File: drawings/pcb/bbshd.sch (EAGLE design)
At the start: 53 parts, among them IC1 LM358D

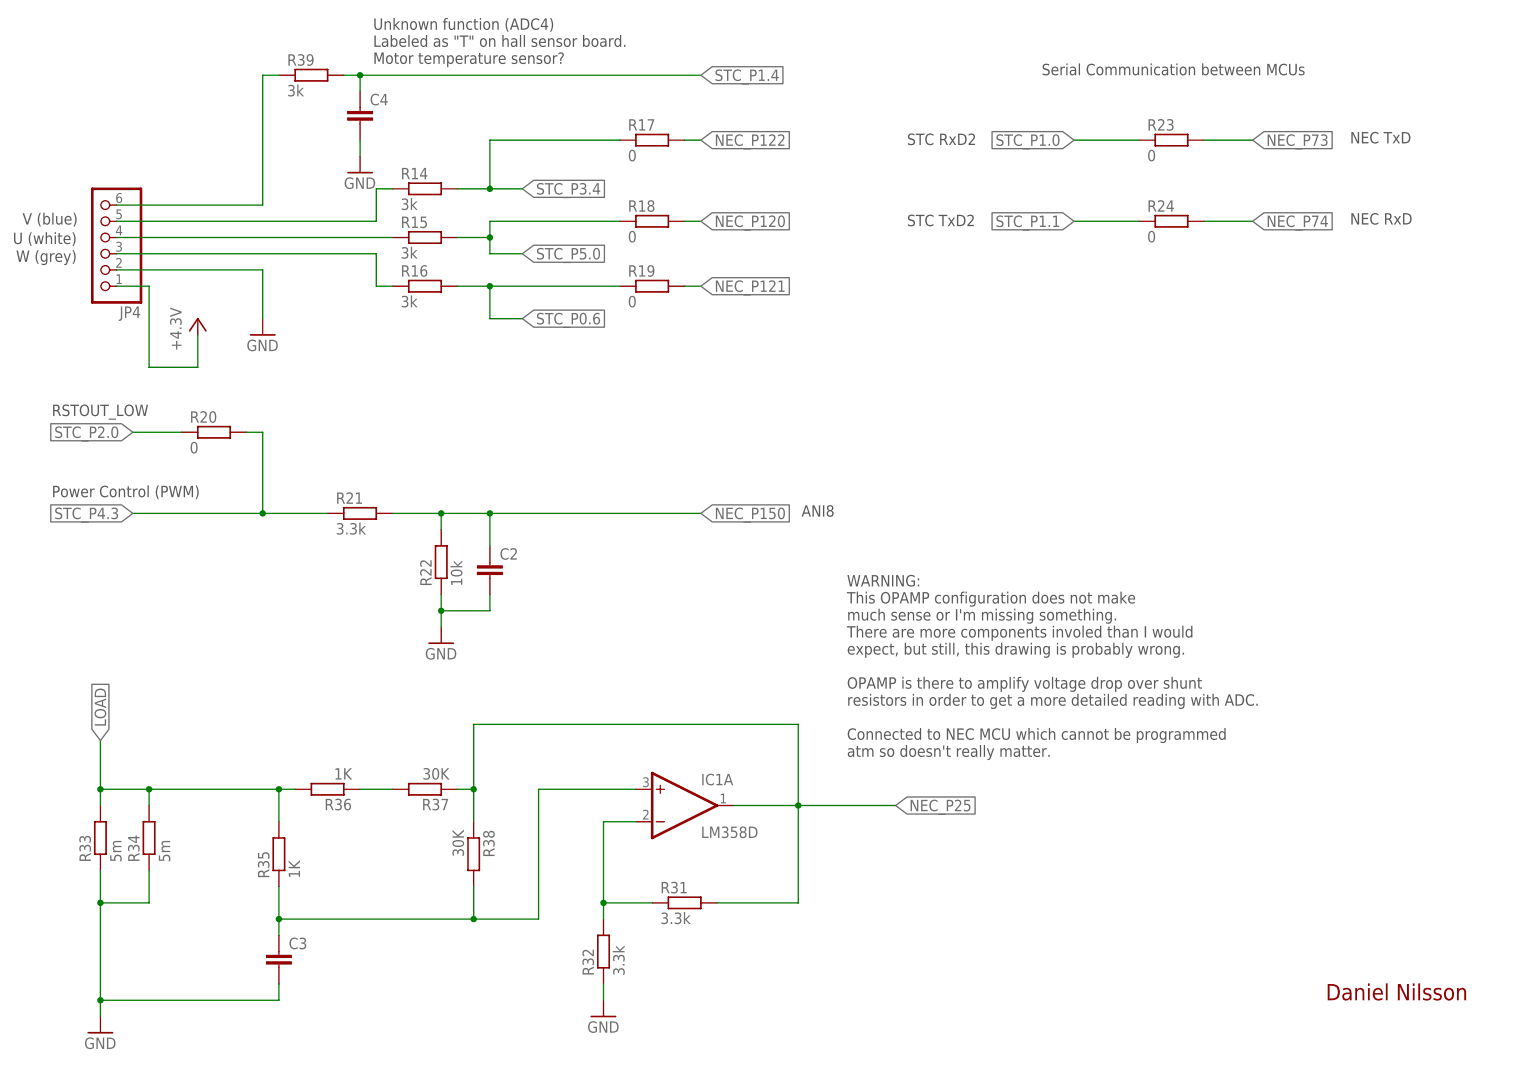
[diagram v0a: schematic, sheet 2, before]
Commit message: Updated shematic for opamp current senser circuit, should be more correct now. Added code dump of 79F9211 ebike controller found on chinese website
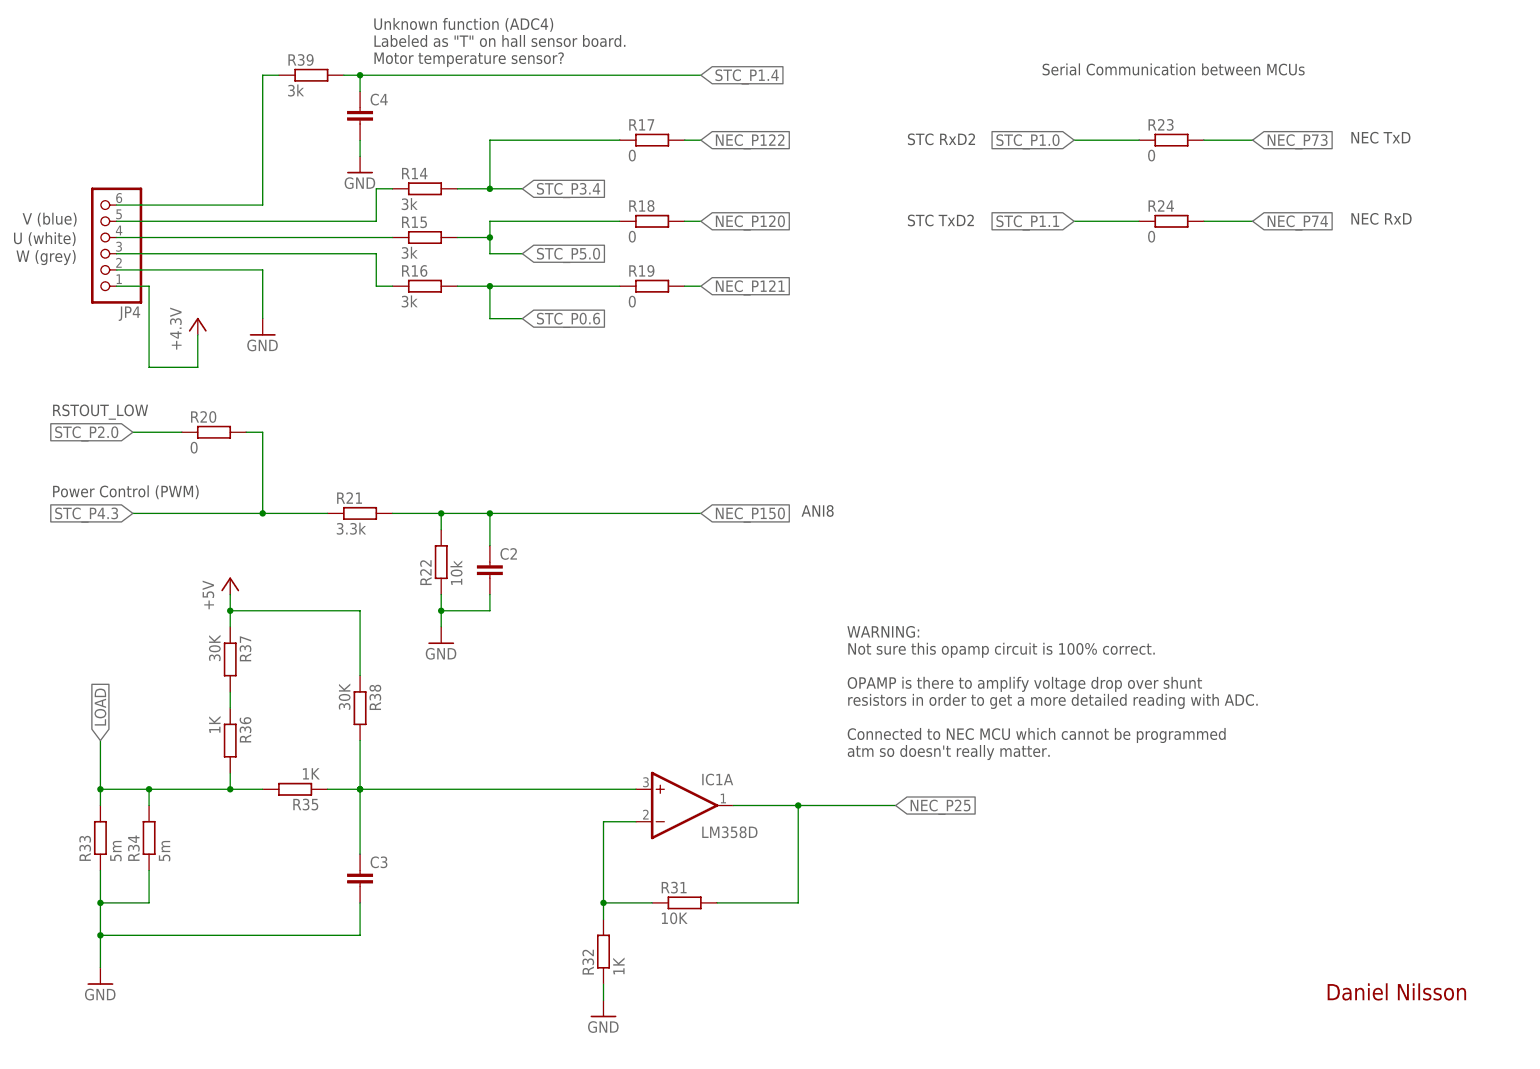
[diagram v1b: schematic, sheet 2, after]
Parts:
- R31: value 3.3k -> 10K
- R32: value 3.3k -> 1K
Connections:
- net +5V: now also R37.1, R38.1
- net NEC_P25: no longer R37.1, R38.1
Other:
- note added: "WARNING: Not sure this opamp circuit is 100% correct. OPAMP is there to amplify voltage drop over shunt resistors in order to get a more detailed reading with ADC. Connected to NEC MCU which cannot be programmed atm so doesn't really matter."
- note removed: "WARNING: This OPAMP configuration does not make much sense or I'm missing something. There are more components involed than I would expect, but still, this drawing is probably wrong. OPAMP is there to amplify voltage drop over shunt resistors in order to get a more detailed reading with ADC. Connected to NEC MCU which cannot be programmed atm so doesn't really matter."
- moved on the sheet: C3, R35, R36, R37, R38
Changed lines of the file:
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@@
 <part name="R30" library="rcl" deviceset="R-EU_" device="R0603" value="2.0K"/>
 <part name="IC1" library="linear" deviceset="LM358" device="D"/>
-<part name="R31" library="rcl" deviceset="R-EU_" device="R0603" value="3.3k"/>
-<part name="R32" library="rcl" deviceset="R-EU_" device="R0603" value="3.3k"/>
+<part name="R31" library="rcl" deviceset="R-EU_" device="R0603" value="10K"/>
+<part name="R32" library="rcl" deviceset="R-EU_" device="R0603" value="1K"/>
 <part name="GND9" library="supply1" deviceset="GND" device=""/>
 <part name="R33" library="rcl" deviceset="R-EU_" device="R0603" value="5m"/>
@@
 <part name="C4" library="rcl" deviceset="C-EU" device="C0603"/>
 <part name="GND11" library="supply1" deviceset="GND" device=""/>
+<part name="P+6" library="supply1" deviceset="+5V" device=""/>
 </parts>
 <sheets>
@@
 <text x="217.17" y="20.32" size="2.54" layer="94">Daniel Nilsson</text>
 <text x="142.24" y="58.42" size="1.778" layer="97">WARNING:
-This OPAMP configuration does not make
-much sense or I'm missing something.
-There are more components involed than I would
-expect, but still, this drawing is probably wrong.
+Not sure this opamp circuit is 100% correct.
 OPAMP is there to amplify voltage drop over shunt
 resistors in order to get a more detailed reading with ADC.
@@
 <instance part="R33" gate="G$1" x="25.4" y="45.72" rot="R90"/>
 <instance part="R34" gate="G$1" x="33.02" y="45.72" rot="R90"/>
-<instance part="GND10" gate="1" x="25.4" y="15.24"/>
-<instance part="C3" gate="G$1" x="53.34" y="27.94"/>
-<instance part="R35" gate="G$1" x="53.34" y="43.18" rot="R90"/>
-<instance part="R36" gate="G$1" x="60.96" y="53.34" rot="R180"/>
-<instance part="R37" gate="G$1" x="76.2" y="53.34" rot="R180"/>
-<instance part="R38" gate="G$1" x="83.82" y="43.18" rot="R270"/>
+<instance part="GND10" gate="1" x="25.4" y="22.86"/>
+<instance part="C3" gate="G$1" x="66.04" y="40.64"/>
+<instance part="R35" gate="G$1" x="55.88" y="53.34" rot="R180"/>
+<instance part="R36" gate="G$1" x="45.72" y="60.96" rot="R270"/>
+<instance part="R37" gate="G$1" x="45.72" y="73.66" rot="R270"/>
+<instance part="R38" gate="G$1" x="66.04" y="66.04" rot="R270"/>
 <instance part="R39" gate="G$1" x="58.42" y="165.1"/>
 <instance part="C4" gate="G$1" x="66.04" y="160.02"/>
 <instance part="GND11" gate="1" x="66.04" y="149.86"/>
+<instance part="P+6" gate="1" x="45.72" y="86.36"/>
 </instances>
 <busses>
@@
 <wire x1="25.4" y1="35.56" x2="25.4" y2="40.64" width="0.1524" layer="91"/>
 <pinref part="GND10" gate="1" pin="GND"/>
-<wire x1="25.4" y1="35.56" x2="25.4" y2="20.32" width="0.1524" layer="91"/>
+<wire x1="25.4" y1="35.56" x2="25.4" y2="30.48" width="0.1524" layer="91"/>
 <junction x="25.4" y="35.56"/>
+<wire x1="25.4" y1="30.48" x2="25.4" y2="25.4" width="0.1524" layer="91"/>
+<wire x1="66.04" y1="30.48" x2="25.4" y2="30.48" width="0.1524" layer="91"/>
+<junction x="25.4" y="30.48"/>
 <pinref part="C3" gate="G$1" pin="2"/>
-<wire x1="25.4" y1="20.32" x2="25.4" y2="17.78" width="0.1524" layer="91"/>
-<wire x1="53.34" y1="22.86" x2="53.34" y2="20.32" width="0.1524" layer="91"/>
-<wire x1="53.34" y1="20.32" x2="25.4" y2="20.32" width="0.1524" layer="91"/>
-<junction x="25.4" y="20.32"/>
+<wire x1="66.04" y1="35.56" x2="66.04" y2="30.48" width="0.1524" layer="91"/>
 </segment>
 <segment>
@@
 <wire x1="25.4" y1="50.8" x2="25.4" y2="53.34" width="0.1524" layer="91"/>
 <junction x="25.4" y="53.34"/>
+<junction x="33.02" y="53.34"/>
+<wire x1="45.72" y1="55.88" x2="45.72" y2="53.34" width="0.1524" layer="91"/>
 <pinref part="R36" gate="G$1" pin="2"/>
-<wire x1="55.88" y1="53.34" x2="53.34" y2="53.34" width="0.1524" layer="91"/>
-<junction x="33.02" y="53.34"/>
 <pinref part="R35" gate="G$1" pin="2"/>
-<wire x1="53.34" y1="53.34" x2="33.02" y2="53.34" width="0.1524" layer="91"/>
-<wire x1="53.34" y1="48.26" x2="53.34" y2="53.34" width="0.1524" layer="91"/>
-<junction x="53.34" y="53.34"/>
-</segment>
-</net>
-<net name="N$19" class="0">
-<segment>
-<pinref part="R36" gate="G$1" pin="1"/>
-<pinref part="R37" gate="G$1" pin="2"/>
-<wire x1="66.04" y1="53.34" x2="71.12" y2="53.34" width="0.1524" layer="91"/>
+<wire x1="45.72" y1="53.34" x2="33.02" y2="53.34" width="0.1524" layer="91"/>
+<wire x1="50.8" y1="53.34" x2="45.72" y2="53.34" width="0.1524" layer="91"/>
+<junction x="45.72" y="53.34"/>
 </segment>
 </net>
 <net name="NEC_P25" class="0">
 <segment>
-<pinref part="R37" gate="G$1" pin="1"/>
-<wire x1="81.28" y1="53.34" x2="83.82" y2="53.34" width="0.1524" layer="91"/>
-<pinref part="R38" gate="G$1" pin="1"/>
-<wire x1="83.82" y1="53.34" x2="83.82" y2="48.26" width="0.1524" layer="91"/>
-<wire x1="83.82" y1="53.34" x2="83.82" y2="63.5" width="0.1524" layer="91"/>
-<junction x="83.82" y="53.34"/>
 <pinref part="IC1" gate="A" pin="OUT"/>
 <wire x1="124.46" y1="50.8" x2="134.62" y2="50.8" width="0.1524" layer="91"/>
@@
 <pinref part="R31" gate="G$1" pin="2"/>
 <wire x1="134.62" y1="35.56" x2="121.92" y2="35.56" width="0.1524" layer="91"/>
-<wire x1="83.82" y1="63.5" x2="134.62" y2="63.5" width="0.1524" layer="91"/>
-<wire x1="134.62" y1="63.5" x2="134.62" y2="50.8" width="0.1524" layer="91"/>
 <junction x="134.62" y="50.8"/>
 <wire x1="134.62" y1="50.8" x2="149.86" y2="50.8" width="0.1524" layer="91"/>
 <label x="149.86" y="50.8" size="1.778" layer="95" xref="yes"/>
-</segment>
-</net>
-<net name="N$21" class="0">
-<segment>
-<pinref part="R38" gate="G$1" pin="2"/>
-<wire x1="83.82" y1="38.1" x2="83.82" y2="33.02" width="0.1524" layer="91"/>
-<wire x1="83.82" y1="33.02" x2="53.34" y2="33.02" width="0.1524" layer="91"/>
-<pinref part="R35" gate="G$1" pin="1"/>
-<pinref part="C3" gate="G$1" pin="1"/>
-<wire x1="53.34" y1="38.1" x2="53.34" y2="33.02" width="0.1524" layer="91"/>
-<wire x1="53.34" y1="33.02" x2="53.34" y2="30.48" width="0.1524" layer="91"/>
-<junction x="53.34" y="33.02"/>
-<pinref part="IC1" gate="A" pin="+IN"/>
-<wire x1="109.22" y1="53.34" x2="93.98" y2="53.34" width="0.1524" layer="91"/>
-<wire x1="93.98" y1="53.34" x2="93.98" y2="33.02" width="0.1524" layer="91"/>
-<wire x1="93.98" y1="33.02" x2="83.82" y2="33.02" width="0.1524" layer="91"/>
-<junction x="83.82" y="33.02"/>
 </segment>
 </net>
@@
 </segment>
 </net>
+<net name="N$18" class="0">
+<segment>
+<pinref part="R37" gate="G$1" pin="2"/>
+<pinref part="R36" gate="G$1" pin="1"/>
+<wire x1="45.72" y1="68.58" x2="45.72" y2="66.04" width="0.1524" layer="91"/>
+</segment>
+</net>
+<net name="+5V" class="0">
+<segment>
+<pinref part="P+6" gate="1" pin="+5V"/>
+<pinref part="R37" gate="G$1" pin="1"/>
+<wire x1="45.72" y1="83.82" x2="45.72" y2="81.28" width="0.1524" layer="91"/>
+<pinref part="R38" gate="G$1" pin="1"/>
+<wire x1="45.72" y1="81.28" x2="45.72" y2="78.74" width="0.1524" layer="91"/>
+<wire x1="66.04" y1="71.12" x2="66.04" y2="81.28" width="0.1524" layer="91"/>
+<wire x1="66.04" y1="81.28" x2="45.72" y2="81.28" width="0.1524" layer="91"/>
+<junction x="45.72" y="81.28"/>
+</segment>
+</net>
+<net name="N$19" class="0">
+<segment>
+<pinref part="C3" gate="G$1" pin="1"/>
+<pinref part="R35" gate="G$1" pin="1"/>
+<wire x1="60.96" y1="53.34" x2="66.04" y2="53.34" width="0.1524" layer="91"/>
+<pinref part="R38" gate="G$1" pin="2"/>
+<wire x1="66.04" y1="53.34" x2="66.04" y2="43.18" width="0.1524" layer="91"/>
+<wire x1="66.04" y1="60.96" x2="66.04" y2="53.34" width="0.1524" layer="91"/>
+<junction x="66.04" y="53.34"/>
+<wire x1="66.04" y1="53.34" x2="109.22" y2="53.34" width="0.1524" layer="91"/>
+<junction x="66.04" y="53.34"/>
+<pinref part="IC1" gate="A" pin="+IN"/>
+</segment>
+</net>

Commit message: Add more relevant documentation for 79F9211 controller. Updated schematic drawing with motor enable signal. Added some original bafang firmware dumps.
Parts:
- added LED1: (no value), led:LED
- added R40: 5.6K, rcl:R-EU_R0603
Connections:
- new net N$20: LED1.C, R40.1
- new net NEC_P70: R40.2
- net +5V: now also LED1.A
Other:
- note added: "Active High"
- note added: "Motor Enable"
- note added: "Some form of status LED. Seems to be blinking during normal operation."
- note removed: "ANI8"
- note removed: "Power Control (PWM)"
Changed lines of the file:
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@@
 <part name="GND11" library="supply1" deviceset="GND" device=""/>
 <part name="P+6" library="supply1" deviceset="+5V" device=""/>
+<part name="P+7" library="supply1" deviceset="+5V" device=""/>
+<part name="R40" library="rcl" deviceset="R-EU_" device="R0603" value="5.6K"/>
+<part name="LED1" library="led" deviceset="LED" device=""/>
 </parts>
 <sheets>
@@
 <text x="13.208" y="141.732" size="1.778" layer="97">V (blue)</text>
 <text x="12.192" y="135.89" size="1.778" layer="97">W (grey)</text>
-<text x="17.78" y="99.06" size="1.778" layer="97">Power Control (PWM)</text>
+<text x="17.78" y="99.06" size="1.778" layer="97">Motor Enable</text>
 <text x="17.78" y="111.76" size="1.778" layer="97">RSTOUT_LOW</text>
-<text x="135.128" y="96.012" size="1.778" layer="97">ANI8</text>
 <text x="220.98" y="154.432" size="1.778" layer="97">NEC TxD</text>
 <text x="151.638" y="154.178" size="1.778" layer="97">STC RxD2</text>
@@
 Labeled as "T" on hall sensor board.
 Motor temperature sensor?</text>
+<text x="165.1" y="127" size="1.778" layer="97">Some form of status LED.
+Seems to be blinking during normal operation.</text>
+<text x="120.65" y="102.108" size="1.778" layer="97">Active High</text>
 </plain>
 <instances>
@@
 <instance part="GND11" gate="1" x="66.04" y="149.86"/>
 <instance part="P+6" gate="1" x="45.72" y="86.36"/>
+<instance part="P+7" gate="1" x="154.94" y="127"/>
+<instance part="R40" gate="G$1" x="193.04" y="119.38"/>
+<instance part="LED1" gate="G$1" x="165.1" y="119.38" rot="R90"/>
 </instances>
 <busses>
@@
 <junction x="45.72" y="81.28"/>
 </segment>
+<segment>
+<pinref part="P+7" gate="1" pin="+5V"/>
+<wire x1="154.94" y1="124.46" x2="154.94" y2="119.38" width="0.1524" layer="91"/>
+<pinref part="LED1" gate="G$1" pin="A"/>
+<wire x1="154.94" y1="119.38" x2="162.56" y2="119.38" width="0.1524" layer="91"/>
+</segment>
 </net>
 <net name="N$19" class="0">
@@
 </segment>
 </net>
+<net name="N$20" class="0">
+<segment>
+<pinref part="LED1" gate="G$1" pin="C"/>
+<pinref part="R40" gate="G$1" pin="1"/>
+<wire x1="170.18" y1="119.38" x2="187.96" y2="119.38" width="0.1524" layer="91"/>
+</segment>
+</net>
+<net name="NEC_P70" class="0">
+<segment>
+<pinref part="R40" gate="G$1" pin="2"/>
+<wire x1="198.12" y1="119.38" x2="205.74" y2="119.38" width="0.1524" layer="91"/>
+<label x="205.74" y="119.38" size="1.778" layer="95" xref="yes"/>
+</segment>
+</net>
